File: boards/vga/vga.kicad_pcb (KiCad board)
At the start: 2 copper layers, 100 x 100 mm, 71 parts, among them J1 Conn_02x20_Odd_Even, J2 L77HDE15SD1CH4RHNVGA, Q1 BSS84AK, U1 SN74LV161APW, U10 62256-TSOP, U11 SN74LV161APW, U12 SN74LV161APW, U13 SN74LV244APW, U14 SN74LV20APW, U15 74LV32APWJ, U16 74LV08APWJ, U17 AT28C256-PLCC32, U18 SN74LV273APW, U19 SN74LV273APW, U2 SN74LV161APW, U20 CD74AC151M96, U21 SN74LV157APW, U22 SN74LV10APW, U23 SN74LV74APW, U24 SN74LV00APW, U25 74LV32APWJ, U26 SN74LV21APW, U27 SN74AHC1G86DBVR, U28 74LV32APWJ, U29 74LV08APWJ, U3 SN74LV157APW, U30 SN74LV74APW, U4 SN74LV157APW, U5 SN74LV157APW, U6 SN74LV161APW, U7 SN74LV161APW, U8 SN74LV244APW, U9 62256-TSOP, X1 MXO45HS-3C-25M1750

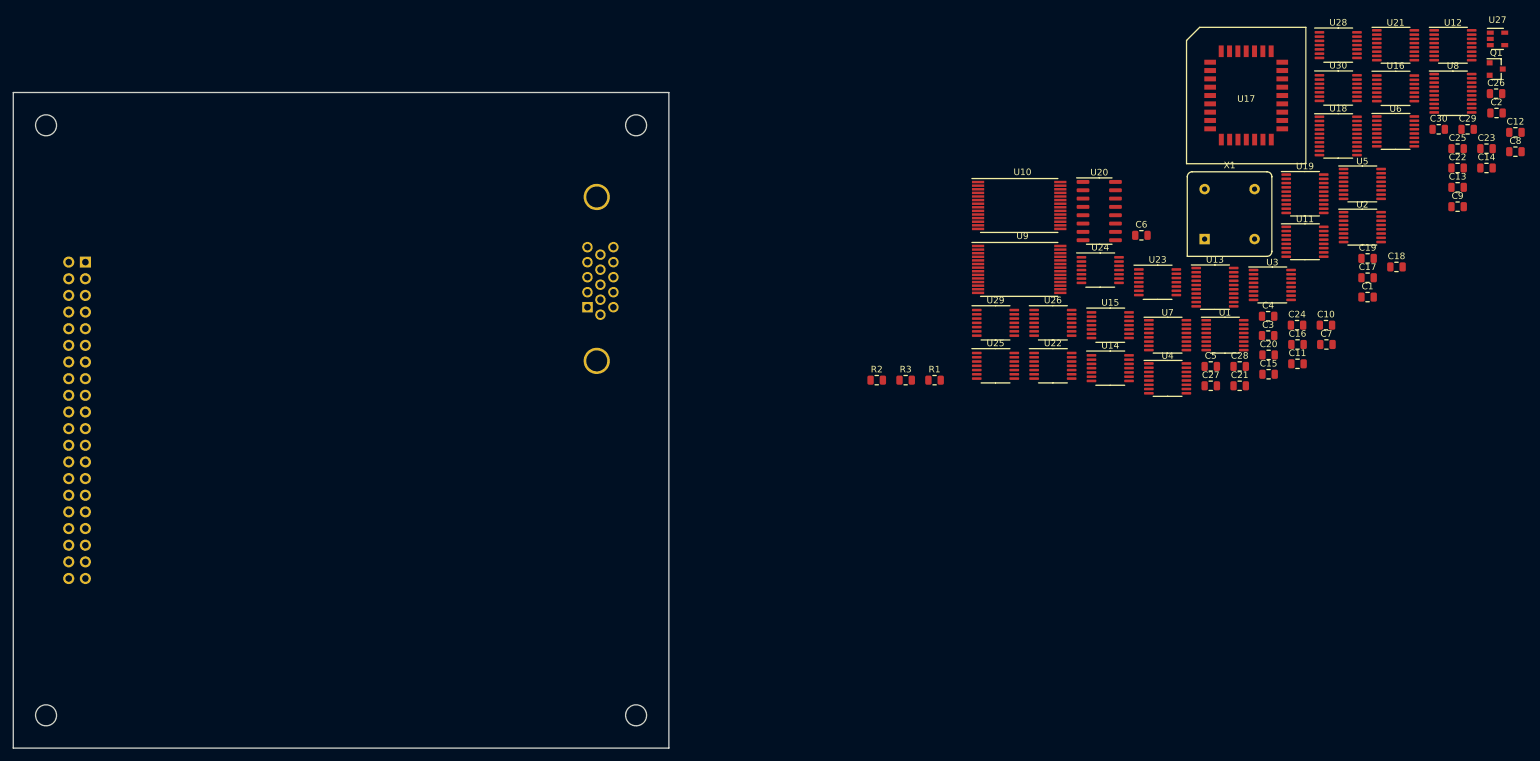
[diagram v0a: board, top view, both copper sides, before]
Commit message: VGA: approx board layout
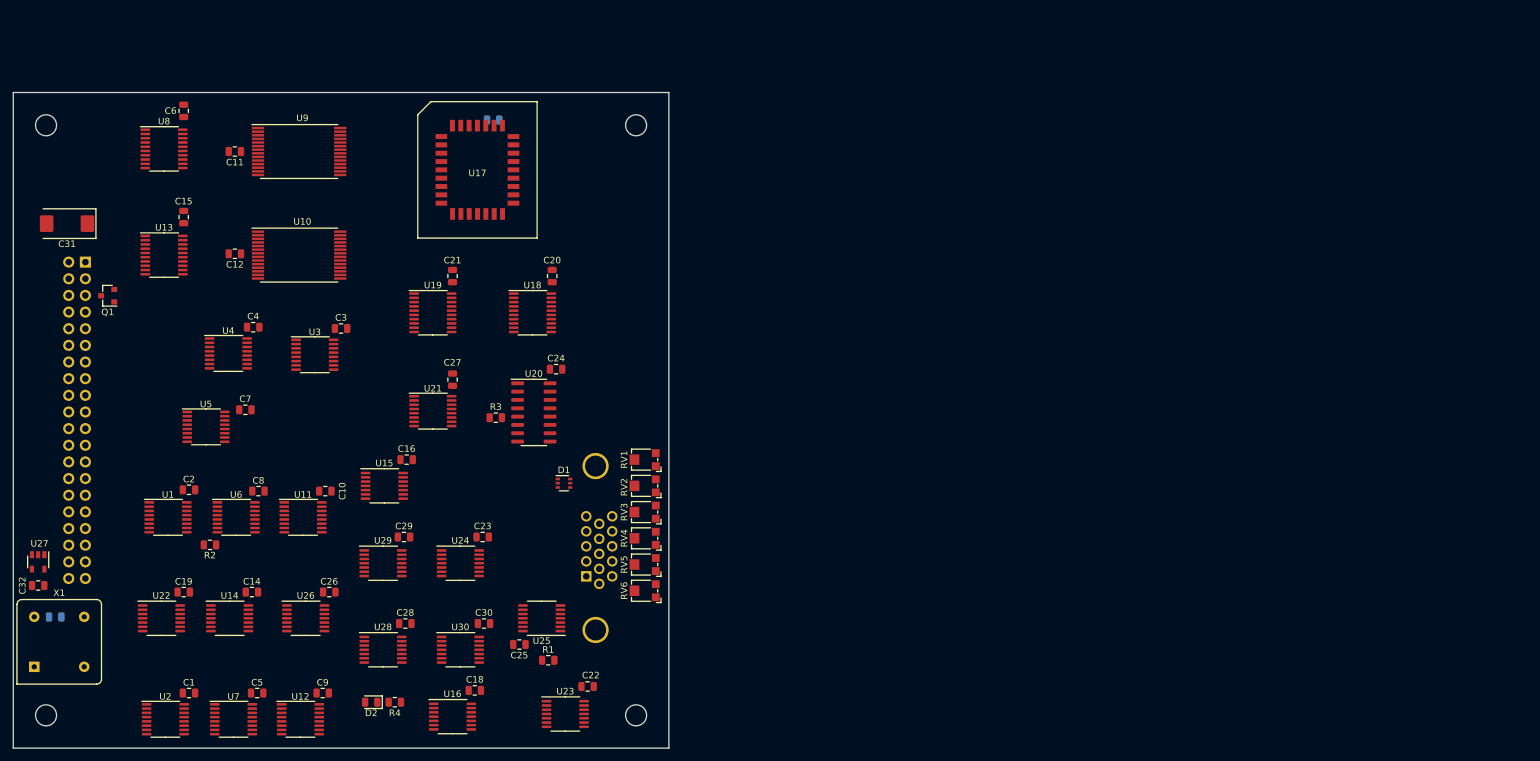
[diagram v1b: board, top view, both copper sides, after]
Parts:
- added C31: TAJD476M016UNJV, Capacitor_Tantalum_SMD:CP_EIA-7343-40_Kemet-Y, F.Cu at (58.2, 70.0)
- added C32: 0.1, Capacitor_SMD:C_0805_2012Metric, F.Cu at (53.8, 125.2)
- added D1: BAS16TW, Package_TO_SOT_SMD:SOT-363_SC-70-6, F.Cu at (134.0, 109.6)
- added D2: LED, LED_SMD:LED_0805_2012Metric, F.Cu at (104.6, 143.0)
- added R4: R, Resistor_SMD:R_0805_2012Metric, F.Cu at (108.2, 143.0)
- added RV1: TC33X-2-102, Potentiometer_SMD:Potentiometer_Bourns_TC33X_Vertical, F.Cu at (146.2, 106.0)
- added RV2: TC33X-2-102, Potentiometer_SMD:Potentiometer_Bourns_TC33X_Vertical, F.Cu at (146.2, 110.0)
- added RV3: TC33X-2-102, Potentiometer_SMD:Potentiometer_Bourns_TC33X_Vertical, F.Cu at (146.2, 114.0)
- added RV4: TC33X-2-102, Potentiometer_SMD:Potentiometer_Bourns_TC33X_Vertical, F.Cu at (146.2, 118.0)
- added RV5: TC33X-2-102, Potentiometer_SMD:Potentiometer_Bourns_TC33X_Vertical, F.Cu at (146.2, 122.0)
- added RV6: TC33X-2-102, Potentiometer_SMD:Potentiometer_Bourns_TC33X_Vertical, F.Cu at (146.2, 126.0)
- C13, C17: moved to B.Cu
- moved U27 236.5 mm to (53.8, 121.6), turned to 270 degrees
- moved C13 223.7 mm to (56.4, 130.0)
- moved Q1 214.6 mm to (64.4, 81.0), turned to 180 degrees
- moved C2 207.6 mm to (76.8, 110.6)
- moved U12 203.6 mm to (93.8, 145.6)
- moved C14 199.1 mm to (86.4, 126.2)
- moved C8 198.6 mm to (87.4, 110.8)
- moved U2 197.4 mm to (73.2, 145.6)
- moved U8 196.8 mm to (73.0, 58.6)
- moved C12 196.2 mm to (83.8, 74.6), turned to 180 degrees
- moved C26 193.5 mm to (98.2, 126.2)
- moved X1 190.1 mm to (53.2, 137.6)
- moved C1 189.6 mm to (76.8, 141.6)
- moved C9 188.3 mm to (97.2, 141.6)
- moved C19 187.6 mm to (76.0, 126.2)
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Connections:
- J2 pad 0: Net-(J2-Pad0) -> GND
- J2 pad 1: Net-(J2-Pad1) -> /ar
- J2 pad 10: Net-(J2-Pad10) -> GND
- J2 pad 13: Net-(J2-Pad13) -> /hsync_out
- J2 pad 14: Net-(J2-Pad14) -> /vsync_out
- J2 pad 2: Net-(J2-Pad2) -> /ag
- J2 pad 3: Net-(J2-Pad3) -> /ab
- J2 pad 5: Net-(J2-Pad5) -> GND
- J2 pad 6: Net-(J2-Pad6) -> GND
- J2 pad 7: Net-(J2-Pad7) -> GND
- J2 pad 8: Net-(J2-Pad8) -> GND

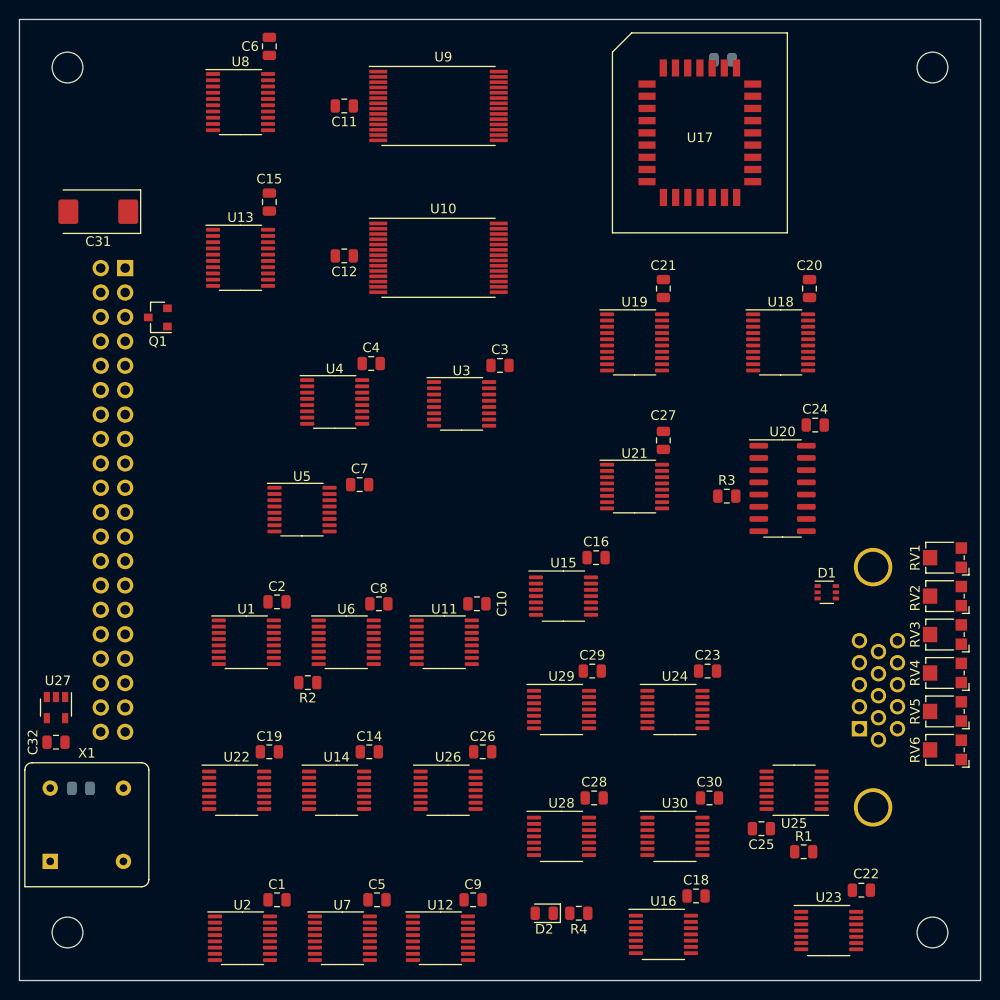
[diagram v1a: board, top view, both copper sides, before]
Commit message: VGA board: power nets
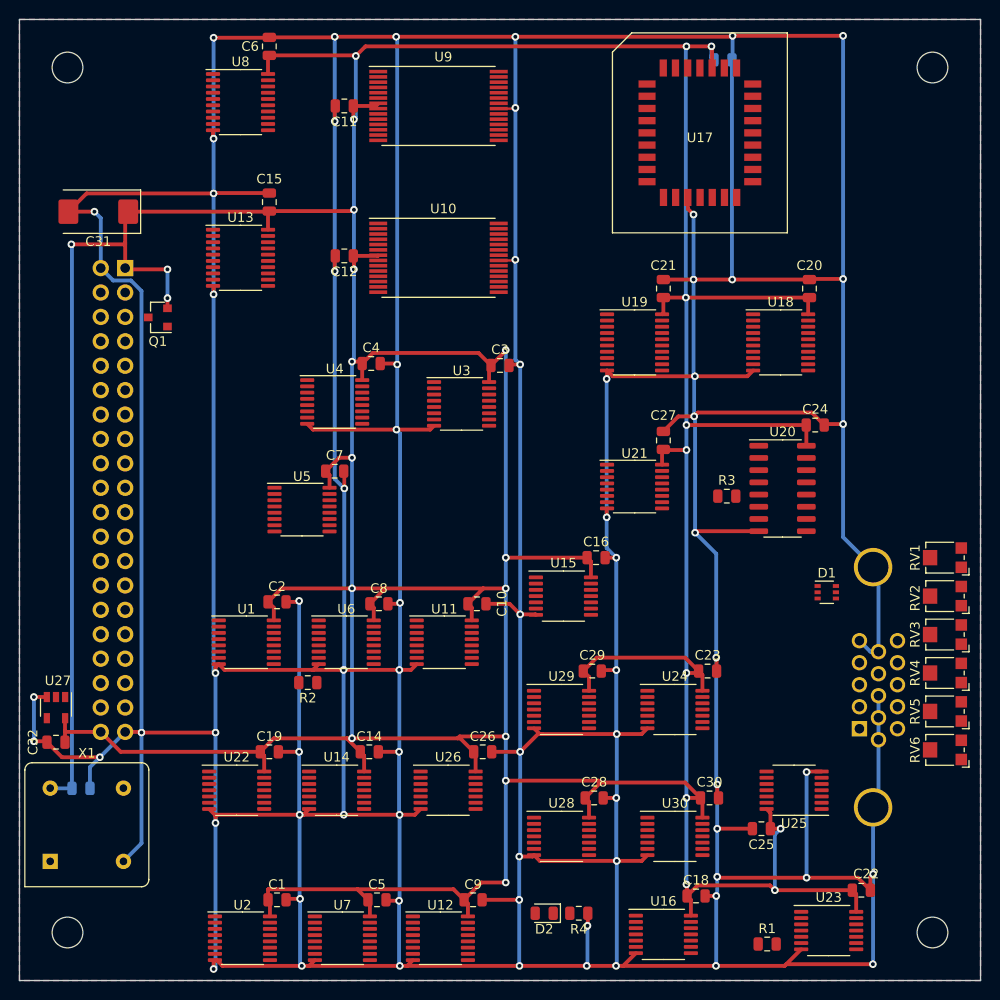
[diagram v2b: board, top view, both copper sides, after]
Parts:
- moved R1 10.3 mm to (127.8, 146.2)
- moved C7 2.95 mm to (82.8, 97.0)
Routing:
- net GND: track 0.00 -> 1179.8 mm, vias 0 -> 72
- net VCC: track 0.00 -> 666.0 mm, vias 0 -> 27
- added copper zone on B.Cu, net GND
- added copper zone on F.Cu, net VCC
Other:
- rule trace_min: 0.2 -> 0.1524

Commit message: VGA board
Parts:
- added R5: 50, Resistor_SMD:R_0805_2012Metric, F.Cu at (124.6, 122.1)
- added R6: 50, Resistor_SMD:R_0805_2012Metric, B.Cu at (73.9, 114.0)
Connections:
- U1 pad 12: /hx2 -> Net-(R6-Pad1)
- U10 pad 14: /char_a3 -> /char_a10
- U10 pad 28: /char_a10 -> /char_a3
- U24 pad 11: /buf_clk -> /~hx2
- U9 pad 14: /char_a3 -> /char_a10
- U9 pad 28: /char_a10 -> /char_a3
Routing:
- net /~rst: track 0.00 -> 196.9 mm, vias 0 -> 11
- net /vy2: track 0.00 -> 191.2 mm, vias 0 -> 12
- net /a_sel: track 0.00 -> 153.7 mm, vias 0 -> 11
- net /vy3: track 0.00 -> 143.7 mm, vias 0 -> 8
- net /~d_to_text_oe: track 0.00 -> 143.2 mm, vias 0 -> 6
- net /vy1: track 0.00 -> 133.0 mm, vias 0 -> 7
- net /hx9: track 0.00 -> 126.7 mm, vias 0 -> 11
- net /vy0: track 0.00 -> 125.9 mm, vias 0 -> 7
- net /a12: track 0.00 -> 125.6 mm, vias 0 -> 7
- net /int_a7: track 0.00 -> 125.4 mm, vias 0 -> 5
- net /~we: track 0.00 -> 117.4 mm, vias 0 -> 4
- net /hx7: track 0.00 -> 111.2 mm, vias 0 -> 9
- net /~h_rst: track 0.00 -> 106.3 mm, vias 0 -> 10
- net VCC: track 666.0 -> 768.3 mm, vias 27 -> 34
- net /~color_ram_we: track 0.00 -> 102.3 mm, vias 0 -> 7
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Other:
- net class Default: clearance 0.2 -> 0.1524; trace_width 0.25 -> 0.16; via_dia 0.8 -> 0.5; via_drill 0.4 -> 0.3
- rule trace_clearance: 0.2 -> 0.1524
- rule via_min_size: 0.4 -> 0.3
- board text added: "Licensed under the TAPR Open Hardware License (www.tapr.org/OHL)"
- board text added: "VGA rev.1"

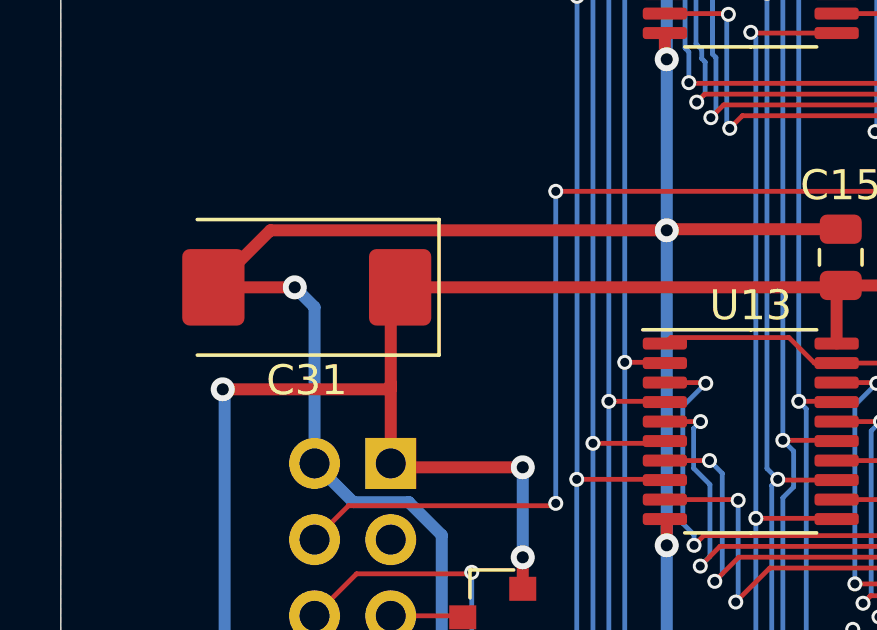
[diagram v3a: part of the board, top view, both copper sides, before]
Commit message: VGA board: change capacitor footprint
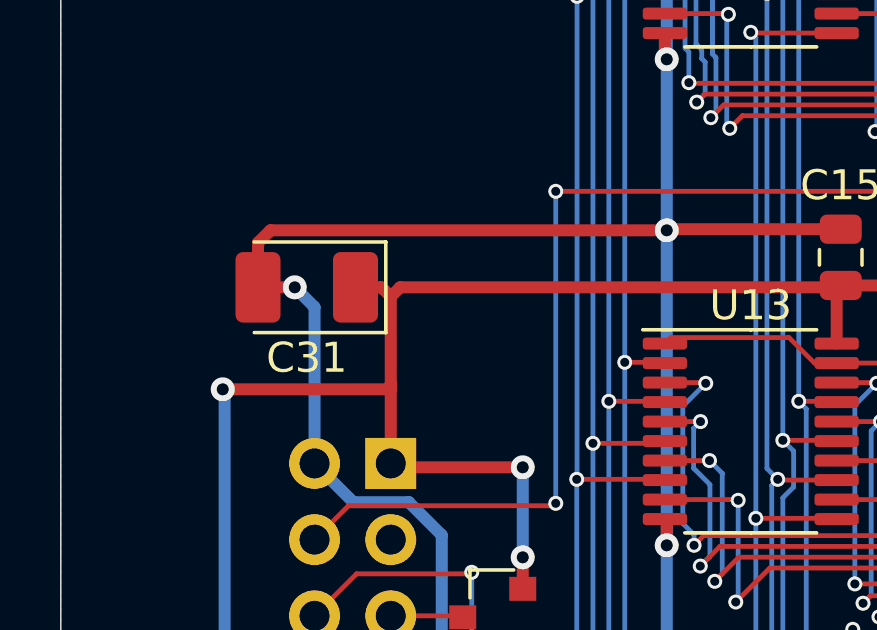
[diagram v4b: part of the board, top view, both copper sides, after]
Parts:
- C31: value TAJD476M016UNJV -> TPSB336K010T0425; footprint Capacitor_Tantalum_SMD:CP_EIA-7343-40_Kemet-Y -> Capacitor_Tantalum_SMD:CP_EIA-3528-15_AVX-H_Pad1.50x2.35mm_HandSolder
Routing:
- net GND: track 1242.9 -> 1240.8 mm
- net VCC: track 768.3 -> 769.6 mm

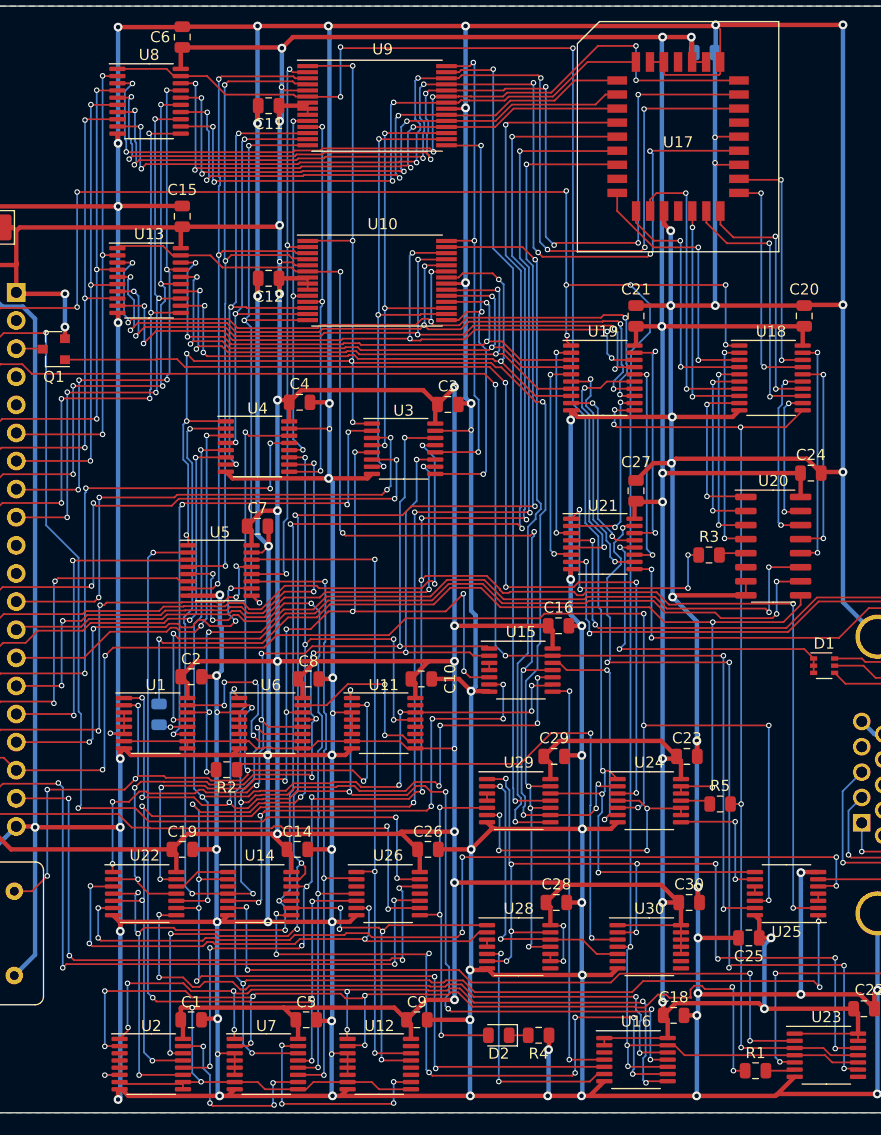
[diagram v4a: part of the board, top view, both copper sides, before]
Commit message: VGA: fix PCB according to schematic amendments
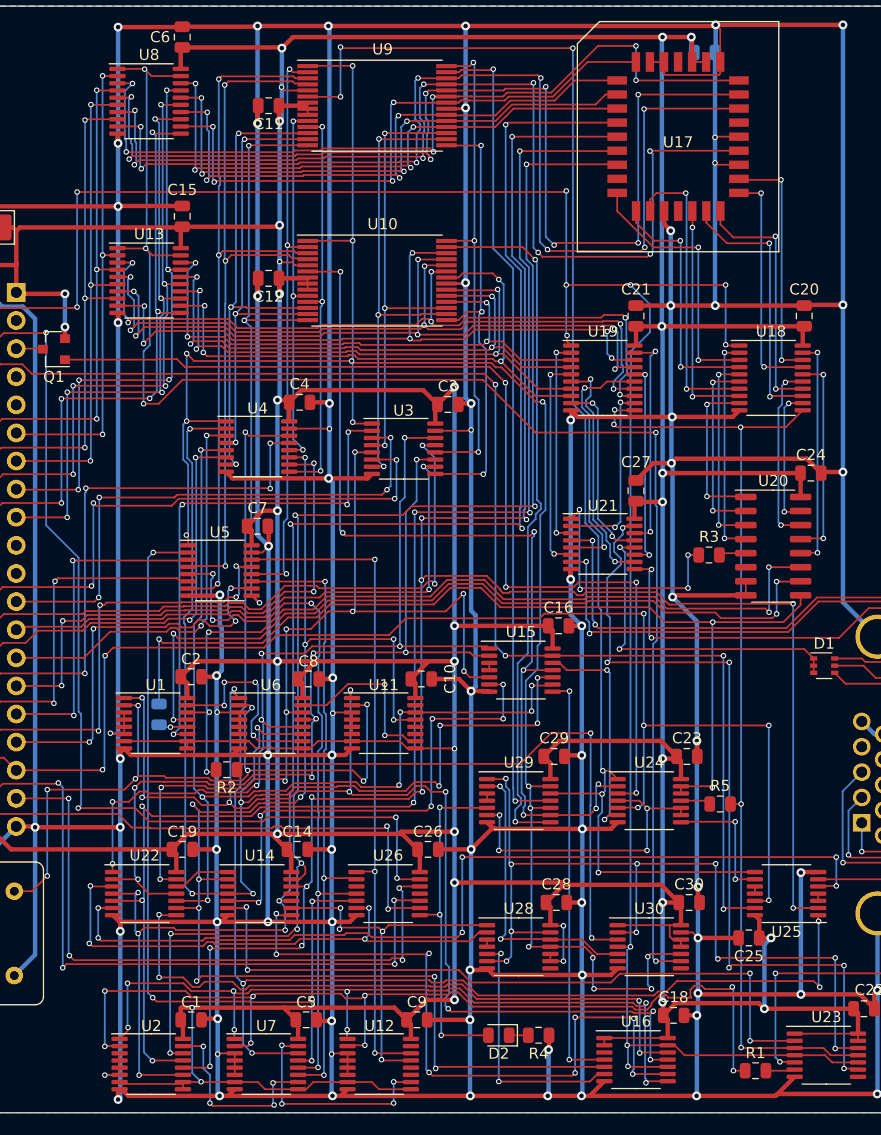
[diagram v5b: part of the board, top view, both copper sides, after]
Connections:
- J1 pad 10: Net-(J1-Pad10) -> (no net)
- J1 pad 19: Net-(J1-Pad19) -> (no net)
- J1 pad 20: Net-(J1-Pad20) -> (no net)
- J1 pad 21: Net-(J1-Pad21) -> (no net)
- J1 pad 22: Net-(J1-Pad22) -> (no net)
- J1 pad 3: Net-(J1-Pad3) -> (no net)
- J1 pad 7: /~oe -> (no net)
- J1 pad 9: Net-(J1-Pad9) -> (no net)
- J2 pad 11: Net-(J2-Pad11) -> (no net)
- J2 pad 12: Net-(J2-Pad12) -> (no net)
- J2 pad 15: Net-(J2-Pad15) -> (no net)
- J2 pad 4: Net-(J2-Pad4) -> (no net)
- J2 pad 9: Net-(J2-Pad9) -> (no net)
- U11 pad 11: Net-(U11-Pad11) -> (no net)
- U11 pad 12: Net-(U11-Pad12) -> (no net)
- U11 pad 15: Net-(U11-Pad15) -> (no net)
- U12 pad 11: Net-(U12-Pad11) -> (no net)
- U12 pad 12: Net-(U12-Pad12) -> (no net)
- U12 pad 15: Net-(U12-Pad15) -> (no net)
- U13 pad 1: /~color_ram_we -> /~a_sel
- U13 pad 19: /~color_ram_we -> /~a_sel
- U16 pad 3: Net-(U16-Pad3) -> (no net)
- U20 pad 6: Net-(U20-Pad6) -> (no net)
- U23 pad 8: /pixel_ena -> (no net)
- U24 pad 1: /~d_to_text_oe -> /~text_ram_we
- U25 pad 8: /~d_to_text_oe -> /~text_ram_we
- U28 pad 8: Net-(U28-Pad8) -> (no net)
- U29 pad 12: /~d_to_text_oe -> /~text_ram_we
- U30 pad 10: VCC -> /a_sel
- U30 pad 13: VCC -> GND
- U30 pad 6: Net-(U30-Pad6) -> (no net)
- U30 pad 8: Net-(U30-Pad8) -> (no net)
- U30 pad 9: Net-(U30-Pad9) -> /~a_sel
- U8 pad 1: /~d_to_text_oe -> /~a_sel
- U8 pad 19: /~d_to_text_oe -> /~a_sel
- U9 pad 6: /~d_to_text_oe -> /~text_ram_we
- X1 pad 1: Net-(X1-Pad1) -> (no net)
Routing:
- net /~d_to_text_oe: track 143.2 -> 0.00 mm, vias 6 -> 0
- net /~a_sel: track 0.00 -> 142.2 mm, vias 0 -> 5
- net /~text_ram_we: track 0.00 -> 124.9 mm, vias 0 -> 6
- net /a_sel: track 153.7 -> 172.3 mm, vias 11 -> 15
- net /~color_ram_we: track 102.3 -> 84.1 mm
- net GND: track 1240.8 -> 1242.5 mm
- net /d6: track 53.2 -> 53.9 mm
- net /stored_color7: track 20.4 -> 19.9 mm
- net /stored_color6: track 19.3 -> 18.8 mm
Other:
- rule via_min_size: 0.3 -> 0.4
